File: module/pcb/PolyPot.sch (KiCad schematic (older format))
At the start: 39 parts, among them J1 V_BAT_1S, J10 I2C_TEST, J2 PROG/DEBUG, J3 HUMIDITY_CONN, J4 TOF_DIST_SENS, J5 M3, J6 M3, J7 M3, J8 M3, J9 LUMINOSITY_CONN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

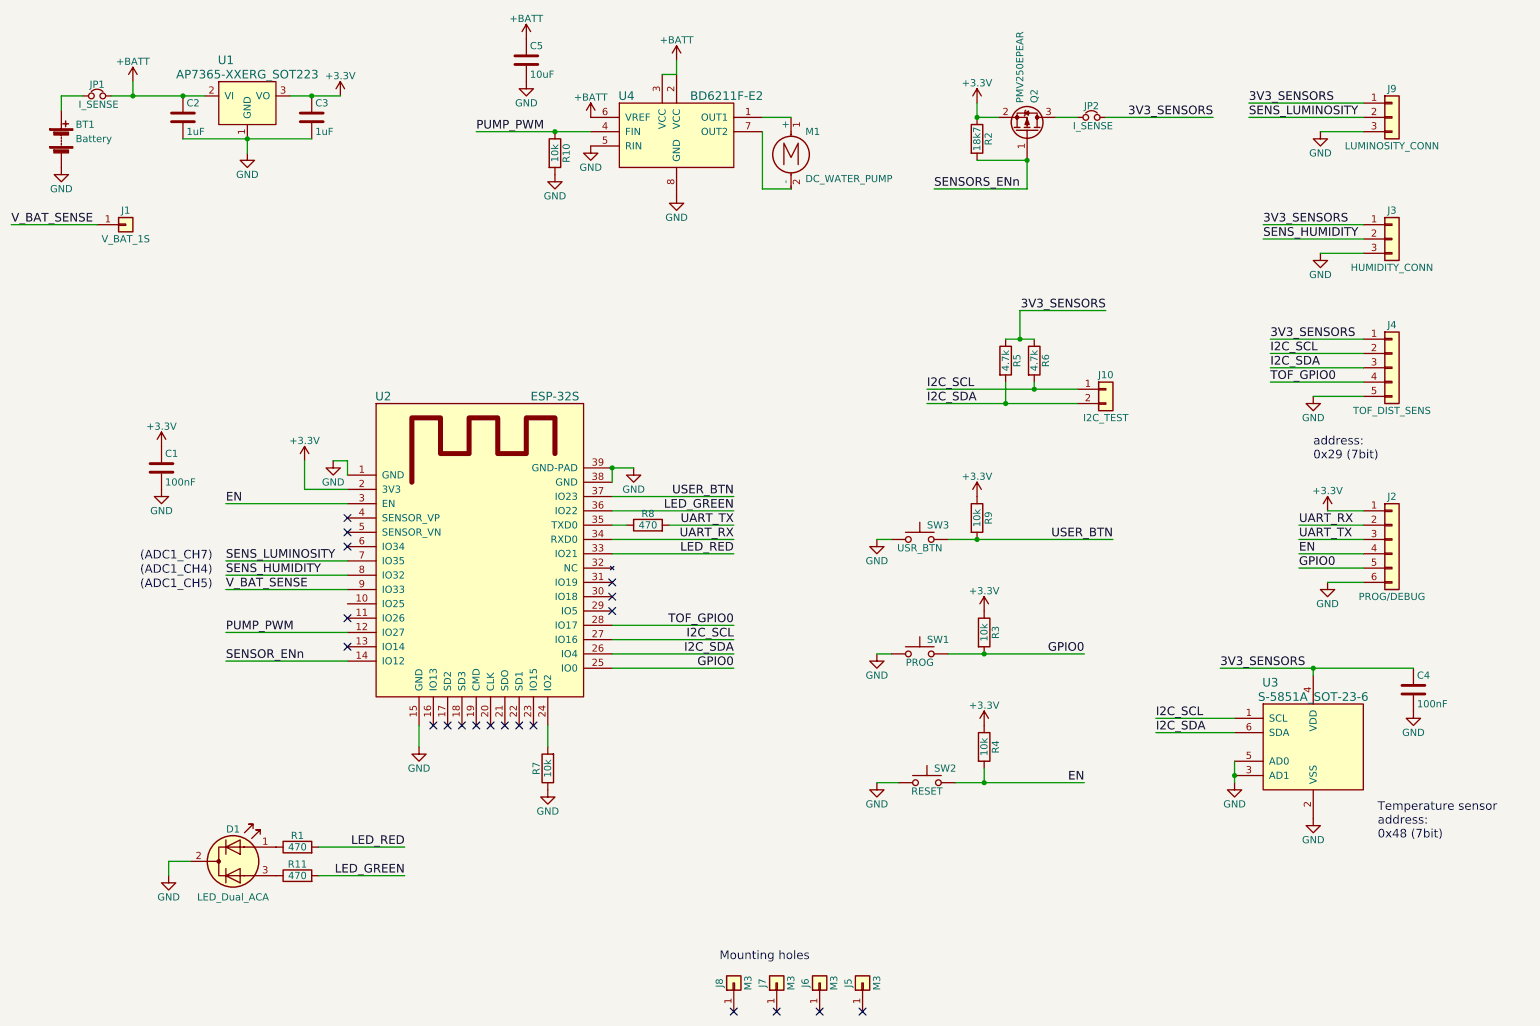
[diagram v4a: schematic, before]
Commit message: PCB: add luminosity sensor to schematic
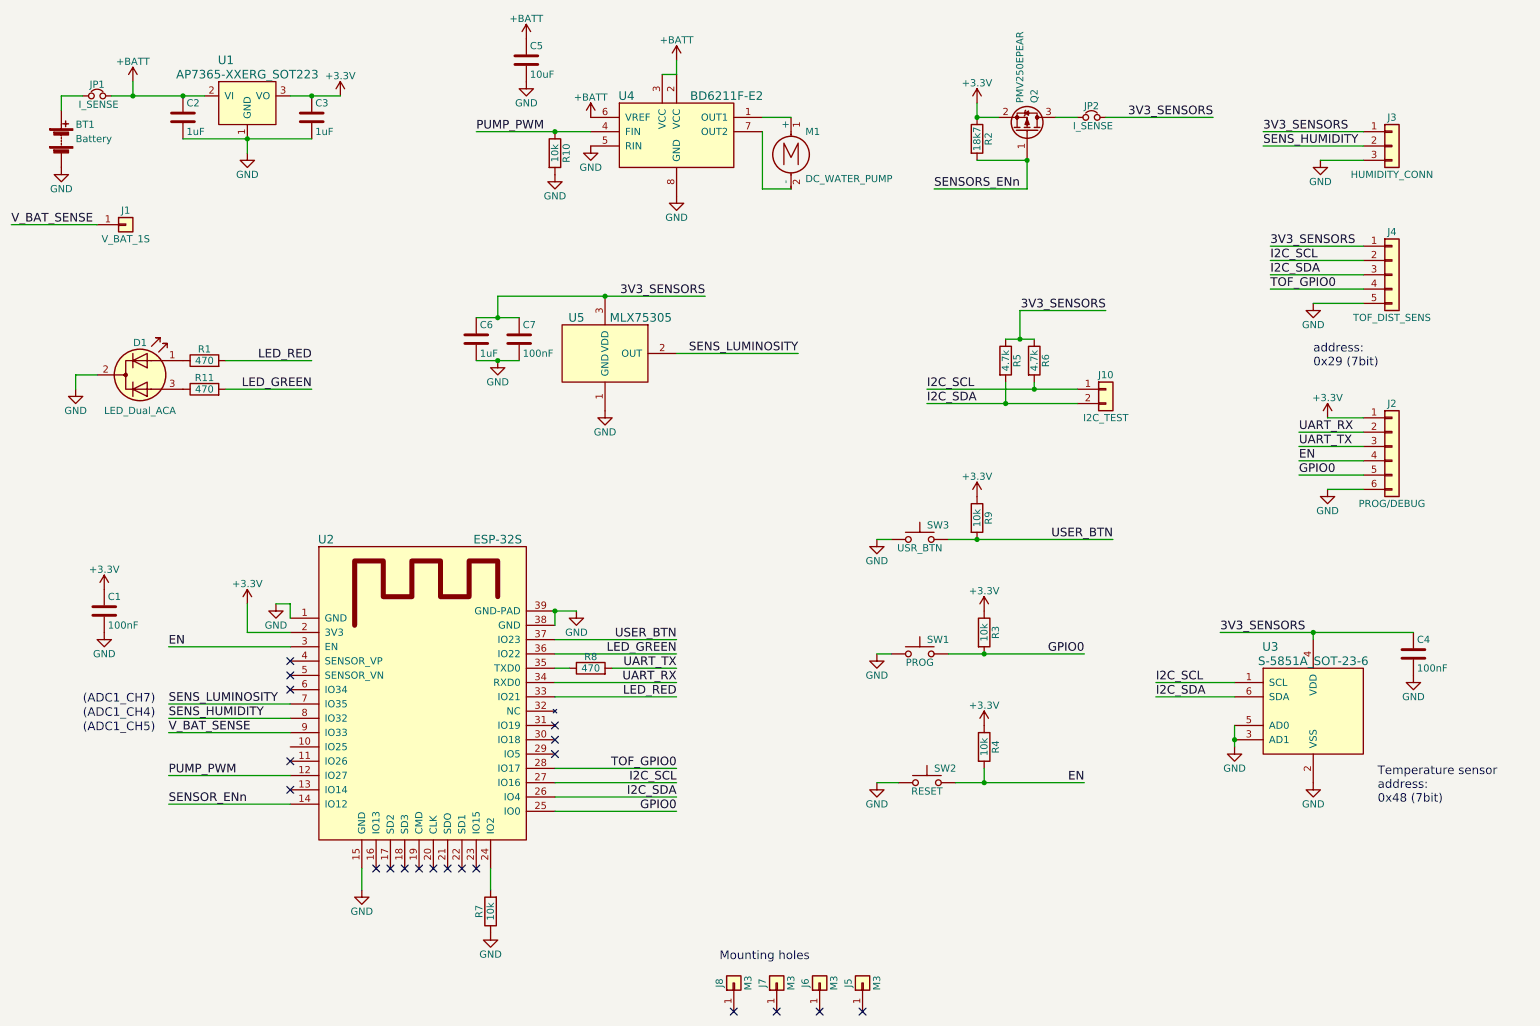
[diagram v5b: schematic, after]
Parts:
- removed J9: LUMINOSITY_CONN, Pin_Headers:Pin_Header_Straight_1x03_Pitch2.54mm, symbol Conn_01x03
- added C6: 1uF, Capacitors_SMD:C_0805_HandSoldering, symbol C
- added C7: 100nF, Capacitors_SMD:C_0603_HandSoldering, symbol C
- added U5: MLX75305, Housings_SOIC:SOIC-8_3.9x4.9mm_Pitch1.27mm, symbol MLX75305
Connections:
- net 3V3_SENSORS: now also C6.1, C7.1, U5.3 (VDD)
- net GND: now also C6.2, C7.2, U5.1 (GND)
- net SENS_LUMINOSITY: now also U5.2 (OUT)
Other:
- moved on the sheet: C1, C4, D1, J2, J3, J4, R1, R11, R7, R8, U2, U3

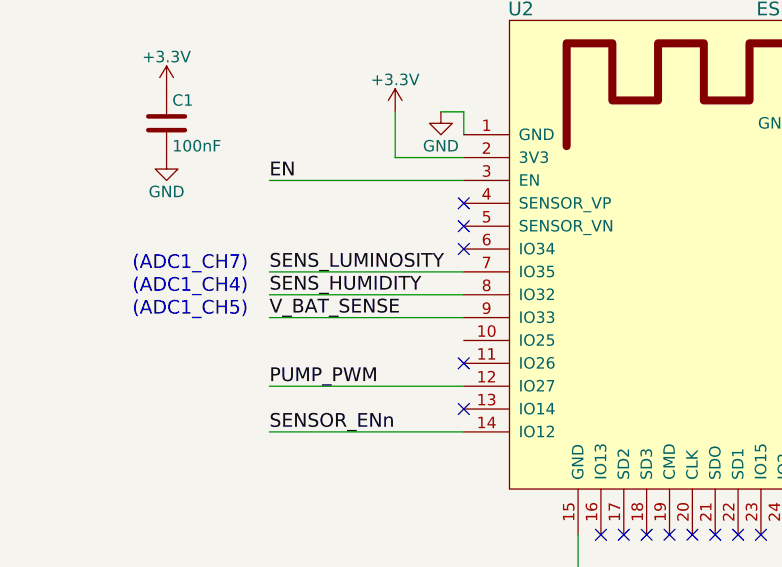
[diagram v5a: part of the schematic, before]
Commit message: PCB: new routing with luminosity sensor, move LED and button to upper side.
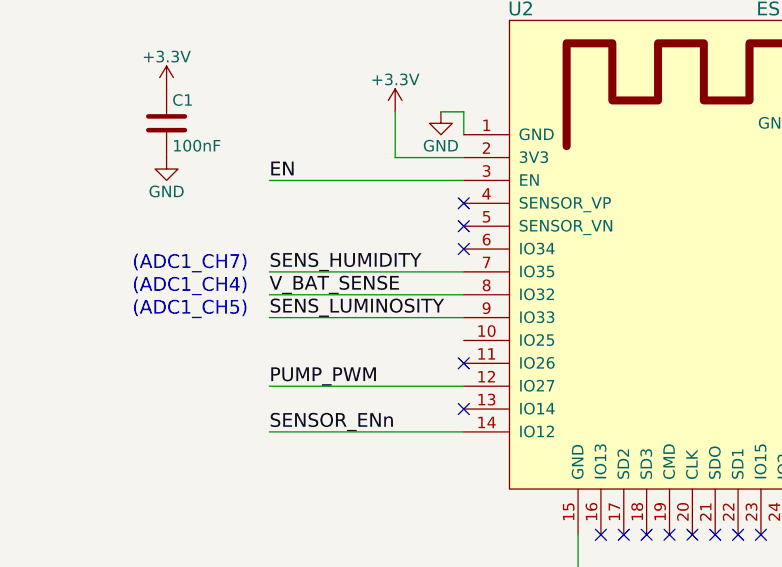
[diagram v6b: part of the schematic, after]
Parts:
- SW3: footprint Buttons_Switches_THT:SW_Tactile_SPST_Angled_PTS645Vx83-2LFS -> Buttons_Switches_SMD:SW_SPST_PTS645
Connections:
- net SENS_HUMIDITY: now also U2.7 (IO35); no longer U2.8 (IO32)
- net SENS_LUMINOSITY: now also U2.9 (IO33); no longer U2.7 (IO35)
- net V_BAT_SENSE: now also U2.8 (IO32); no longer U2.9 (IO33)
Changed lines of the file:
@@
 F 0 "SW3" H 7050 4350 50  0000 L CNN
 F 1 "USR_BTN" H 7000 4190 50  0000 C CNN
-F 2 "Buttons_Switches_THT:SW_Tactile_SPST_Angled_PTS645Vx83-2LFS" H 7000 4450 50  0001 C CNN
+F 2 "Buttons_Switches_SMD:SW_SPST_PTS645" H 7000 4450 50  0001 C CNN
 F 3 "" H 7000 4450 50  0001 C CNN
 	1    7000 4250
@@
 Text Label 1750 5000 0    60   ~ 0
 EN
+Text Label 1750 5500 0    60   ~ 0
+V_BAT_SENSE
+Text Label 1750 5400 0    60   ~ 0
+SENS_HUMIDITY
 Text Label 1750 5600 0    60   ~ 0
-V_BAT_SENSE
-Text Label 1750 5500 0    60   ~ 0
-SENS_HUMIDITY
-Text Label 1750 5400 0    60   ~ 0
 SENS_LUMINOSITY
 Text Label 5300 4950 2    60   ~ 0

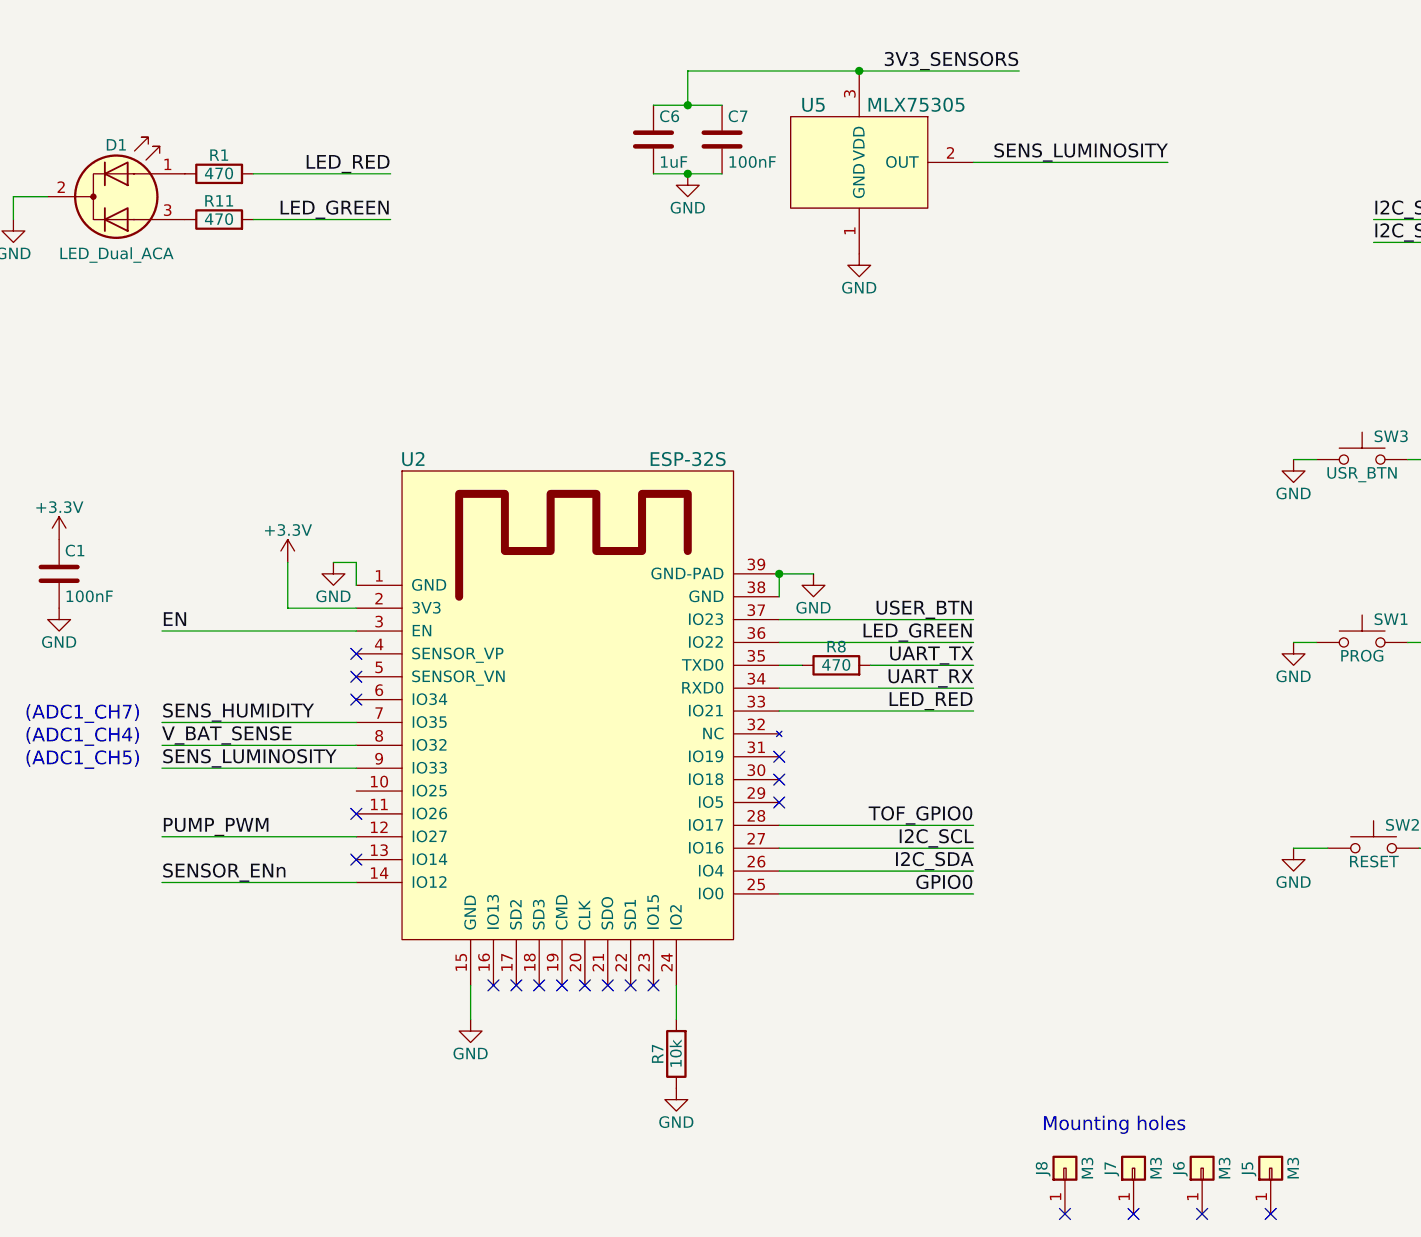
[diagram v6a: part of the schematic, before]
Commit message: Update hardware fixes in schematic
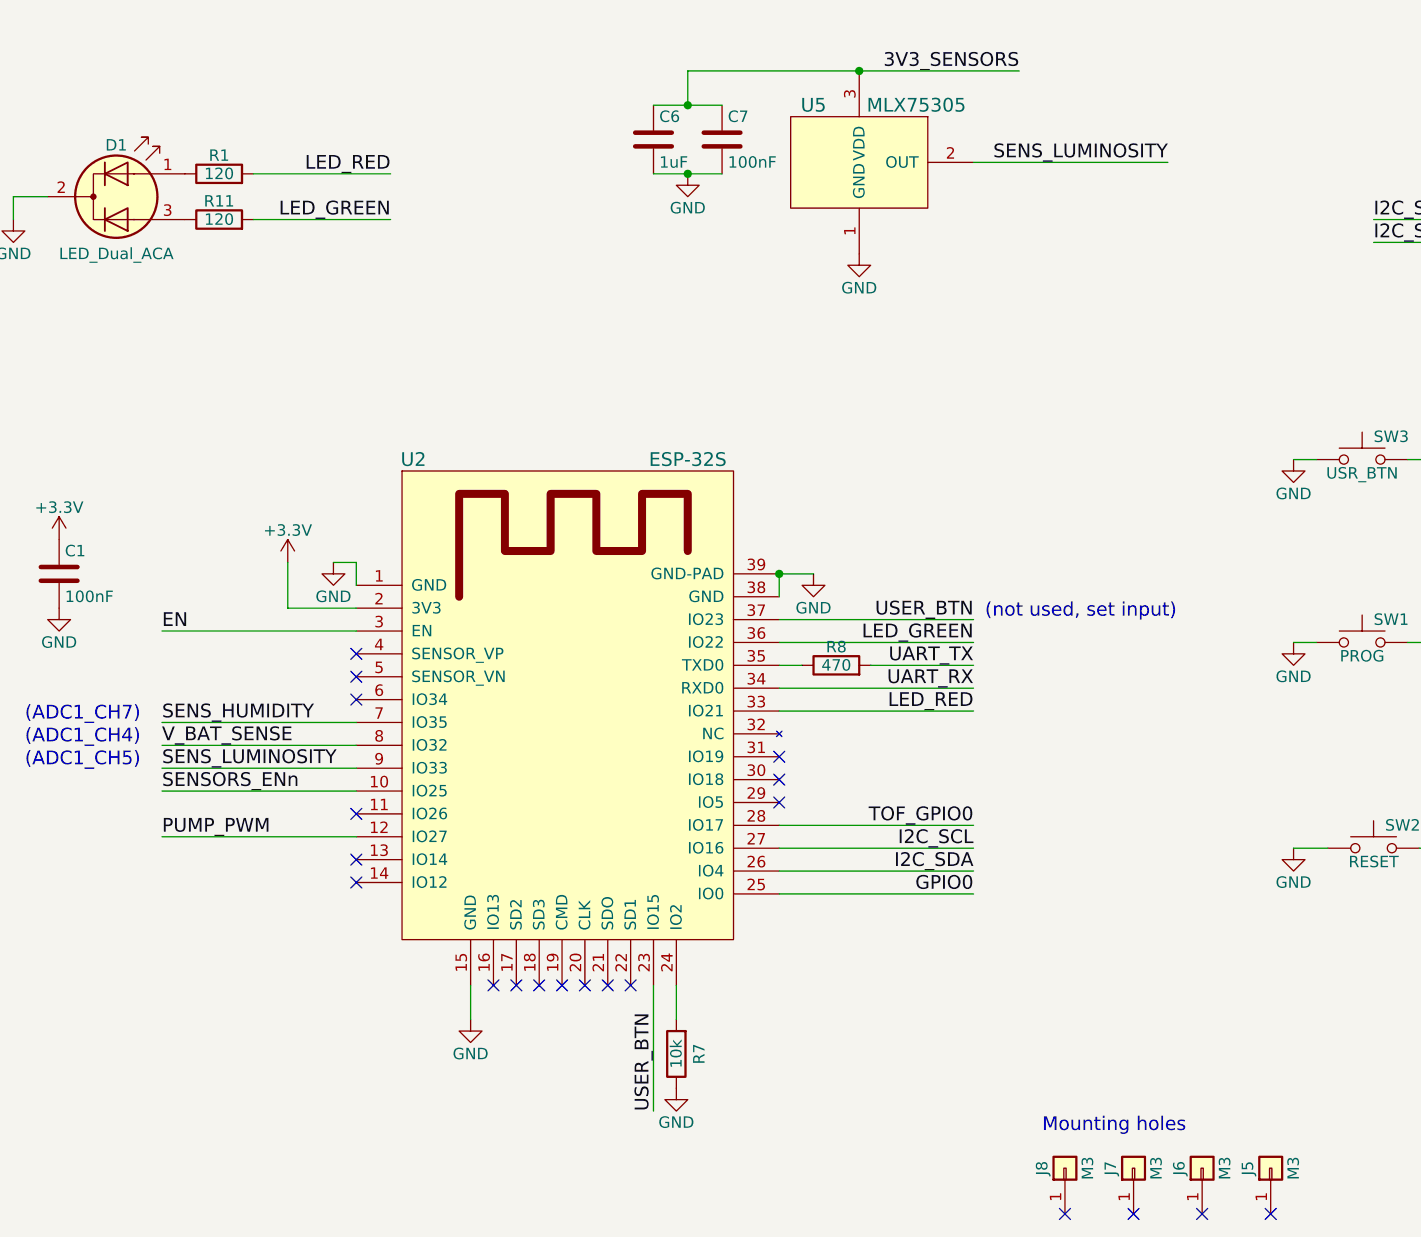
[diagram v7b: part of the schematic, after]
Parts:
- R1, R11: value 470 -> 120
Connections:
- net SENSORS_ENn: now also U2.10 (IO25)
- net USER_BTN: now also U2.23 (IO15)
- net SENSOR_ENn: no longer names the net of U2.14 (IO12)
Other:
- note added: "(not used, set input)"
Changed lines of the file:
@@
 P 2000 3000
 F 0 "R1" V 2080 3000 50  0000 C CNN
-F 1 "470" V 2000 3000 50  0000 C CNN
+F 1 "120" V 2000 3000 50  0000 C CNN
 F 2 "Resistors_SMD:R_0603_HandSoldering" V 1930 3000 50  0001 C CNN
 F 3 "" H 2000 3000 50  0001 C CNN
@@
 U 1 1 5A0B2274
 P 4000 6850
-F 0 "R7" V 4080 6850 50  0000 C CNN
+F 0 "R7" V 3900 6850 50  0000 C CNN
 F 1 "10k" V 4000 6850 50  0000 C CNN
 F 2 "Resistors_SMD:R_0603_HandSoldering" V 3930 6850 50  0001 C CNN
@@
 Text Label 5300 4950 2    60   ~ 0
 USER_BTN
-Text Label 1750 6100 0    60   ~ 0
-SENSOR_ENn
 $Comp
 L GND #PWR026
@@
 P 2000 3200
 F 0 "R11" V 2080 3200 50  0000 C CNN
-F 1 "470" V 2000 3200 50  0000 C CNN
+F 1 "120" V 2000 3200 50  0000 C CNN
 F 2 "Resistors_SMD:R_0603_HandSoldering" V 1930 3200 50  0001 C CNN
 F 3 "" H 2000 3200 50  0001 C CNN
@@
 NoConn ~ 4450 5550
 NoConn ~ 4450 5650
-NoConn ~ 3900 6550
 NoConn ~ 3800 6550
 NoConn ~ 3700 6550
@@
 	4450 5050 5300 5050
 Wire Wire Line
-	1750 6100 2600 6100
+	1750 5700 2600 5700
 Wire Wire Line
 	3100 6550 3100 6700
@@
 Connection ~ 4050 2700
 Connection ~ 4800 2550
+Text Label 1750 5700 0    60   ~ 0
+SENSORS_ENn
+NoConn ~ 2600 6100
+Text Label 3900 7100 1    60   ~ 0
+USER_BTN
+Wire Wire Line
+	3900 7100 3900 6550
+Text Notes 5350 4950 0    60   ~ 0
+(not used, set input)
 $EndSCHEMATC
